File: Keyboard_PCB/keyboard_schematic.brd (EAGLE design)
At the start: 589.5 x 222.5 mm, 260 parts, among them M2 KEYSWITCH-RGBSMDLED-ALPSMX-1U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, M3 KEYSWITCH-RGBSMDLED-ALPSMX-1U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, M4 KEYSWITCH-RGBSMDLED-ALPSMX-1U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, M5 KEYSWITCH-RGBSMDLED-ALPSMX-1U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, M6 KEYSWITCH-RGBSMDLED-ALPSMX-1U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, Y2 CRYSTAL-GROUNDEDSMD-3.2X2.5

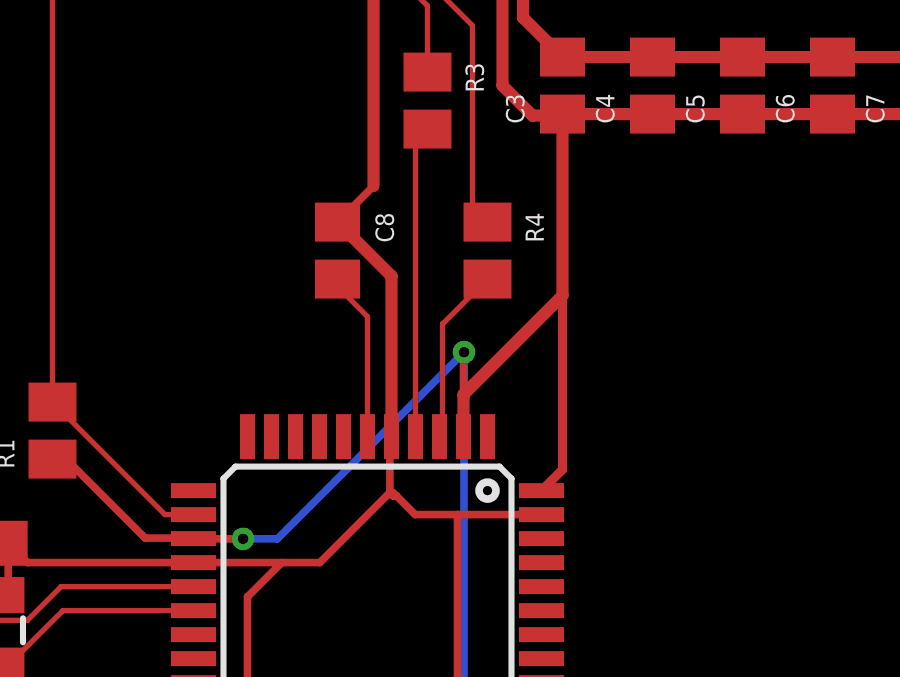
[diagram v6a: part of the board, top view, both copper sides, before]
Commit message: Updated Schematic Names
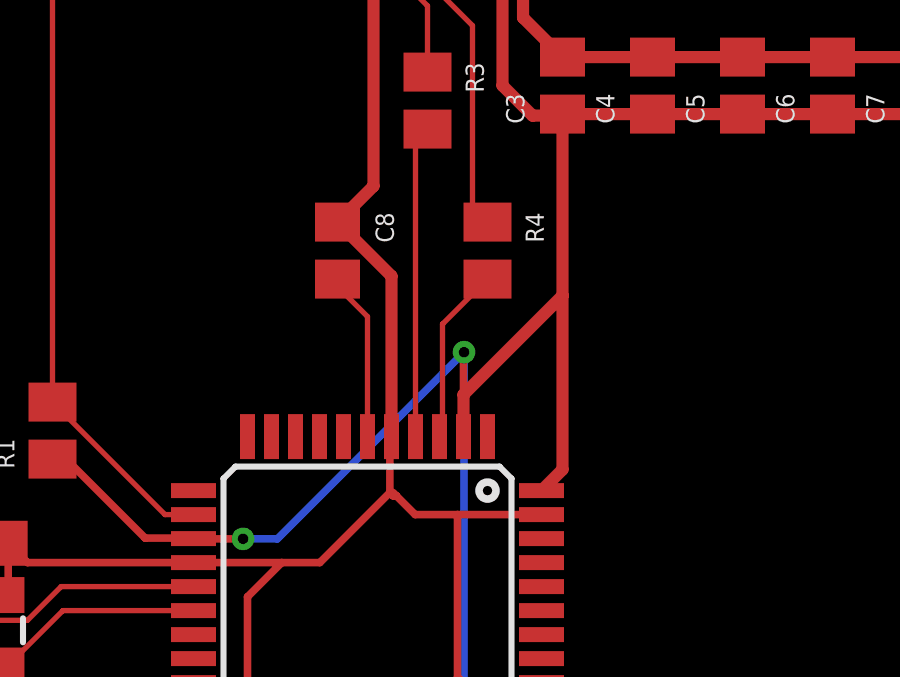
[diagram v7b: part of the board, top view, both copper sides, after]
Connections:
- net N$116 renamed XTAL1
- net N$117 renamed XTAL2
- net N$118 renamed RESET
- net N$119 renamed PE2
- net N$121 renamed D+USB
- net N$122 renamed D-USB
- net N$123 renamed D+32U
- net N$124 renamed D-32U4
- net N$125 renamed UCAP
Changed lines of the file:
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@@
 <wire x1="9.02" y1="110.45" x2="9.06" y2="111.03" width="0" layer="19" extent="1-1"/>
 </signal>
-<signal name="N$116">
+<signal name="XTAL1">
 <contactref element="C1" pad="1"/>
 <contactref element="U$1" pad="17"/>
@@
 <wire x1="397.3468" y1="141.5" x2="401.7" y2="141.5" width="0.1778" layer="1"/>
 </signal>
-<signal name="N$117">
+<signal name="XTAL2">
 <contactref element="C2" pad="1"/>
 <contactref element="U$1" pad="16"/>
@@
 <wire x1="410.5" y1="139.28875" x2="410.5" y2="144.7" width="0.254" layer="1"/>
 <wire x1="407.7" y1="164.775" x2="407.7" y2="155.65" width="0.4064" layer="1"/>
-<wire x1="407.7" y1="155.65" x2="406.5" y2="154.45" width="0.254" layer="1"/>
+<wire x1="407.7" y1="155.65" x2="406.5" y2="154.45" width="0.4064" layer="1"/>
 <wire x1="406.5" y1="154.45" x2="408.3" y2="152.65" width="0.4064" layer="1"/>
 <wire x1="408.3" y1="152.65" x2="408.3" y2="147.3" width="0.4064" layer="1"/>
@@
 <wire x1="397.45486875" y1="146.55" x2="400.08826875" y2="143.9166" width="0.254" layer="1"/>
 <wire x1="410.7" y1="147.3" x2="410.7" y2="148.7" width="0.4064" layer="1"/>
-<wire x1="414" y1="152" x2="414" y2="146.2" width="0.3048" layer="1"/>
-<wire x1="414" y1="146.2" x2="413.3" y2="145.5" width="0.3048" layer="1"/>
+<wire x1="414" y1="152" x2="414" y2="146.2" width="0.4064" layer="1"/>
+<wire x1="414" y1="146.2" x2="413.3" y2="145.5" width="0.4064" layer="1"/>
 <wire x1="410.7" y1="148.7" x2="410.7" y2="150.096" width="0.254" layer="1"/>
 <wire x1="410.7" y1="150.096" x2="410.718" y2="150.114" width="0.254" layer="1"/>
@@
 <wire x1="401.709" y1="143.891" x2="401.7" y2="143.9" width="0.254" layer="1"/>
 </signal>
-<signal name="N$118">
+<signal name="RESET">
 <contactref element="S1" pad="2"/>
 <contactref element="U$1" pad="13"/>
@@
 <wire x1="397" y1="163.484" x2="397" y2="148.45" width="0.1778" layer="1"/>
 </signal>
-<signal name="N$119">
+<signal name="PE2">
 <contactref element="R2" pad="2"/>
 <contactref element="U$1" pad="33"/>
@@
 <wire x1="413.044" y1="135.7" x2="413.118" y2="135.626" width="0.1778" layer="1"/>
 </signal>
-<signal name="N$121">
+<signal name="D+USB">
 <contactref element="J1" pad="D+"/>
 <contactref element="R3" pad="1"/>
@@
 <wire x1="409" y1="162.15875" x2="409.5" y2="161.65875" width="0.1778" layer="1"/>
 </signal>
-<signal name="N$122">
+<signal name="D-USB">
 <contactref element="J1" pad="D-"/>
 <contactref element="R4" pad="1"/>
@@
 <wire x1="411" y1="161" x2="411" y2="154.95" width="0.1778" layer="1"/>
 </signal>
-<signal name="N$123">
+<signal name="D+32U">
 <contactref element="R3" pad="2"/>
 <contactref element="U$1" pad="4"/>
@@
 <wire x1="409.1" y1="157.15" x2="409.1" y2="147.3" width="0.1778" layer="1"/>
 </signal>
-<signal name="N$124">
+<signal name="D-32U4">
 <contactref element="U$1" pad="3"/>
 <contactref element="R4" pad="2"/>
@@
 <wire x1="410" y1="151.05" x2="410" y2="147.4" width="0.1778" layer="1"/>
 </signal>
-<signal name="N$125">
+<signal name="UCAP">
 <contactref element="C8" pad="2"/>
 <contactref element="U$1" pad="6"/>

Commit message: Changed MCU to a larger chip
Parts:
- removed J1: (no value), SparkFun-Connectors:USB-B-MICRO-SMD
- removed U$1: 32U4, SparkFun-IC-Microcontroller:TQFP44
- added IC1: LMV321M5, linear:SOT23-5
- added IC2: (no value), controller-micro_atmel_jd:QFN64
- added R5, R6: 5.1k, rcl:M0805
- added R7: 475, rcl:M0805
- added R8: 150, rcl:M0805
- added T1: BC846, transistor:SOT23
- added U$2: PCB_USB_CDS_1, USB_pcb_connectors:USB_TYPE_C_DS_1
- moved C7 491.2 mm to (-25.7, -34.0), turned to 0 degrees
- moved C3 468.1 mm to (-16.3, -25.4), turned to 0 degrees
- moved R2 465.6 mm to (-17.0, -40.4), turned to 0 degrees
- moved C4 465.5 mm to (-10.4, -25.4), turned to 0 degrees
- moved R3 463.0 mm to (-8.64, -40.4), turned to 0 degrees
- moved C5 462.9 mm to (-4.57, -25.4), turned to 0 degrees
- moved C8 461.9 mm to (-12.7, -40.4), turned to 0 degrees
- moved S1 460.8 mm to (-23.1, -26.7), turned to 0 degrees
- moved C6 460.3 mm to (1.27, -25.4), turned to 0 degrees
- moved R4 459.0 mm to (-4.57, -40.4), turned to 0 degrees
- moved R1 458.6 mm to (-21.3, -40.4), turned to 0 degrees
- moved C1 448.8 mm to (-19.8, -34.0), turned to 0 degrees
- moved C2 446.0 mm to (-14.5, -34.0)
- moved Y2 442.4 mm to (-6.35, -46.0), turned to 0 degrees
- moved DBACKSLASH 1.27 mm to (276.6, 73.4), flipped to the bottom
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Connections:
- new net +5V: IC1.5, IC2.21, IC2.52, IC2.62, IC2.64, R7.2, T1.3, U$2.A4, U$2.A9, U$2.B4, U$2.B9
- new net CC1: R5.1, U$2.A5
- new net CC2: IC1.1, R6.2, U$2.B5
- new net LED_VCC: T1.2
- new net N$116: IC1.3, R7.1, R8.2
- new net N$117: IC1.4, T1.1
- new net UVCC: IC2.3
- net COL1: no longer U$1.36
- net COL10: no longer U$1.31
- net COL11: no longer U$1.27
- net COL12: no longer U$1.1
- net COL2: no longer U$1.37
- net COL3: no longer U$1.38
- net COL4: no longer U$1.39
- net COL5: no longer U$1.40
- net COL6: no longer U$1.41
- net COL7: no longer U$1.19
- net COL8: no longer U$1.18
- net COL9: no longer U$1.25
- net D+32U: now also IC2.5; no longer U$1.4
- net D+USB: now also U$2.A6; no longer J1.D+
- net D-32U4: now also IC2.4; no longer U$1.3
- net D-USB: now also U$2.A7; no longer J1.D-
- net GND: now also IC1.2, IC2.22, IC2.53, IC2.6, IC2.63, R5.2, R6.1, R8.1, U$2.A1, U$2.A12, U$2.B1, U$2.B12; no longer J1.GND, J1.SHIELD1, J1.SHIELD2, J1.SHIELD3, U$1.15, U$1.23, U$1.35, U$1.43, U$1.5
- net PE2: now also IC2.43; no longer U$1.33
- net RESET: now also IC2.20; no longer U$1.13
- net ROW1.1: no longer U$1.28
- net ROW1.2: no longer U$1.29
- net ROW2.1: no longer U$1.30
- net ROW2.2: no longer U$1.12
- net ROW3.1: no longer U$1.26
- net ROW3.2: no longer U$1.32
- net ROW4.1: no longer U$1.8
- net ROW4.2: no longer U$1.9
- net ROW5.1: no longer U$1.10
- net ROW5.2: no longer U$1.11
- net ROW6.1: no longer U$1.22
- net UCAP: now also IC2.7; no longer U$1.6
- net VCC: no longer J1.VBUS, U$1.14, U$1.2, U$1.24, U$1.34, U$1.44
- net XTAL1: now also IC2.24; no longer U$1.17
- net XTAL2: now also IC2.23; no longer U$1.16
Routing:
- net GND: track 112.7 -> 0.00 mm
- net VCC: track 81.7 -> 0.00 mm, vias 3 -> 0
- net RESET: track 26.7 -> 0.00 mm
- net D-USB: track 11.1 -> 0.00 mm
- net XTAL2: track 10.5 -> 0.00 mm
- net D+32U: track 10.4 -> 0.00 mm
- net XTAL1: track 9.23 -> 0.00 mm
- net D-32U4: track 5.91 -> 0.00 mm
- net UCAP: track 5.66 -> 0.00 mm
- net D+USB: track 5.53 -> 0.00 mm
- net PE2: track 1.65 -> 0.00 mm
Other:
- board size 589.5 x 222.5 mm -> 487.7 x 175.3 mm
